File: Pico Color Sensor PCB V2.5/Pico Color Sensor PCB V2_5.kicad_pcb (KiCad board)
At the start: 4 copper layers, 62.2 x 85.7 mm, 16 parts

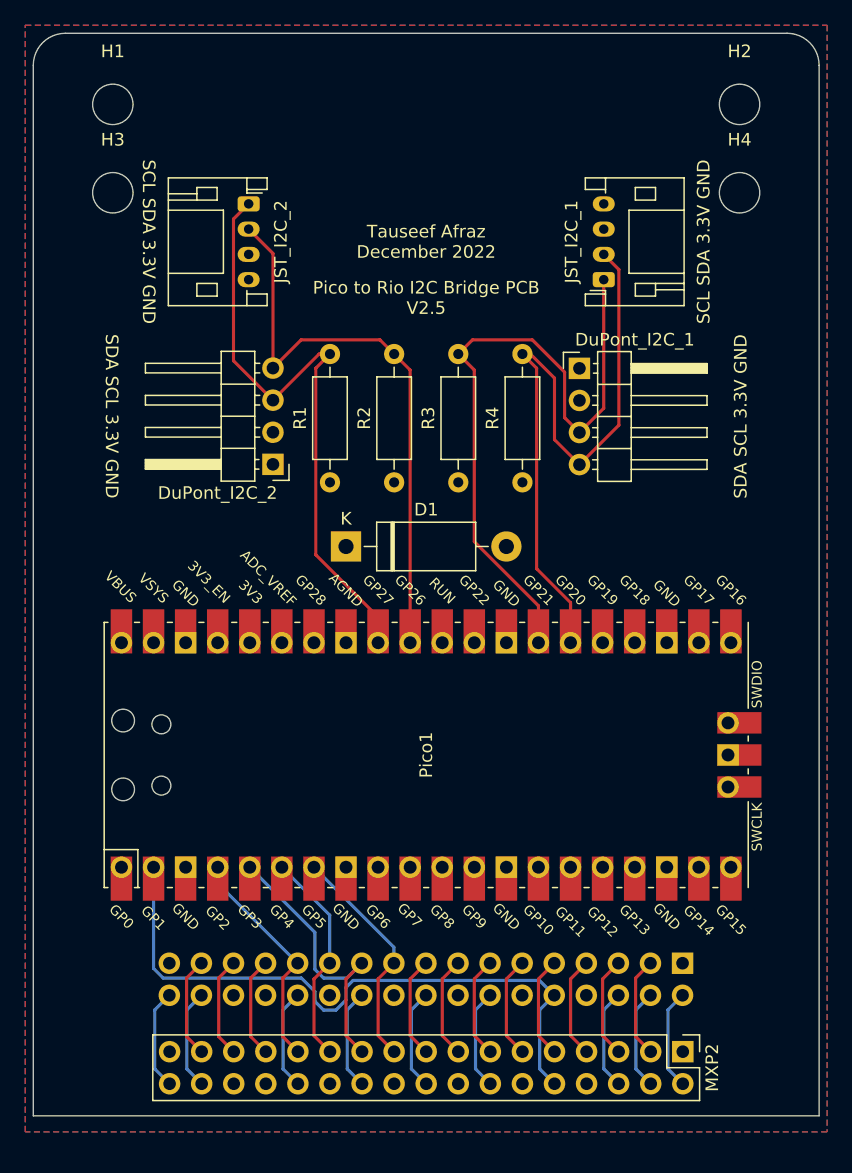
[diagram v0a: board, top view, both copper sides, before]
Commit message: Made V2.5 board a bit longer
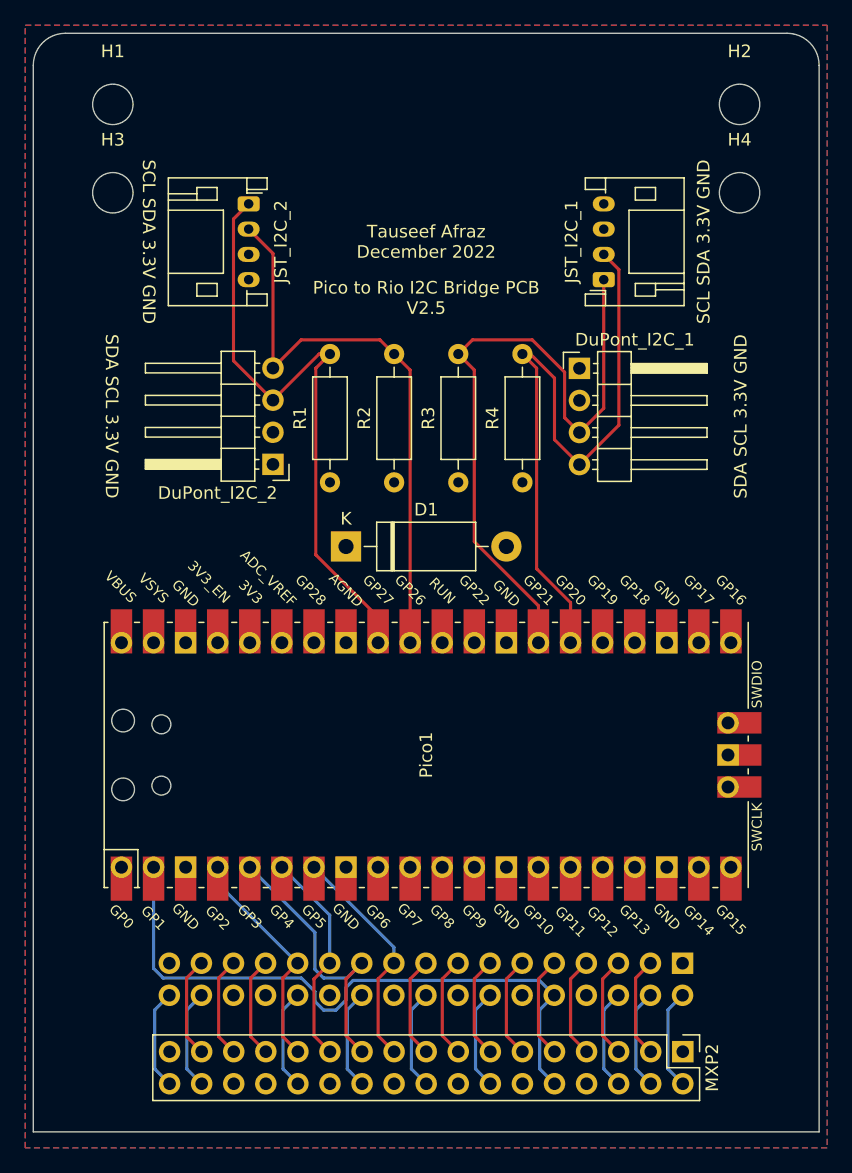
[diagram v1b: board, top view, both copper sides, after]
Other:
- board size 62.2 x 85.7 mm -> 62.2 x 87 mm
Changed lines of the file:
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@@
   (gr_line (start 184.785 65.405) (end 127.635 65.405) (layer "Edge.Cuts") (width 0.1))
   (gr_arc (start 184.785 65.405) (mid 186.581051 66.148949) (end 187.325 67.945) (layer "Edge.Cuts") (width 0.1))
-  (gr_line (start 125.095 151.13) (end 125.095 67.945) (layer "Edge.Cuts") (width 0.1))
-  (gr_line (start 187.325 67.945) (end 187.325 151.13) (layer "Edge.Cuts") (width 0.1))
-  (gr_line (start 187.325 151.13) (end 125.095 151.13) (layer "Edge.Cuts") (width 0.1))
+  (gr_line (start 125.095 152.4) (end 125.095 67.945) (layer "Edge.Cuts") (width 0.1))
+  (gr_line (start 187.325 67.945) (end 187.325 152.4) (layer "Edge.Cuts") (width 0.1))
+  (gr_line (start 187.325 152.4) (end 125.095 152.4) (layer "Edge.Cuts") (width 0.1))
   (gr_text "tauseefafraz.com" (at 156.21 108.585) (layer "B.SilkS")
     (effects (font (size 1 1) (thickness 0.15)) (justify mirror))
@@
     (polygon
       (pts
-        (xy 187.96 152.4)
-        (xy 124.46 152.4)
+        (xy 187.96 153.67)
+        (xy 124.46 153.67)
         (xy 124.46 64.77)
         (xy 187.96 64.77)
